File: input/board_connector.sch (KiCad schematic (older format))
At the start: 1 part

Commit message: Still beating into overall shape.  This is a checkpoint before modifying the analog signal chain to fold the diff amp and antialias into the driver, going to a full differential path.
Overall: Changes to component attributes to reduce duplicates in BOM, and added links to Digikey and datasheets.

board_connector.sch: Added reference input pins, decimation SEL lines.

in_filter.sch:
Fixed BIST feedback to be taken at the top of each injection resistor (4 lines, not 2)

input_board.sch:
Added some missing connections and no-connects.

power_budget.xlsx:
Much more elaborate now, models effect of input levels on load currents, computes currents and total power, for several variants.

reference_buffer.sch:
Updated with booster sink transistor to handle sourcing into reference by ADC clamp diodes.

simetrix/:
Added supply_negative.wxsch and supply_positive.wxsch, which are concepts for low noise lowish dropout regulators for the analog rails.  Other simetrix modifications are cosmetic.
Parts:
- J2: renamed from J?; footprint Connector_PinHeader_2.54mm:PinHeader_2x32_P2.54mm_Vertical -> Connector_DIN:DIN41612_B_2x32_Horizontal; Description (none) -> 64 Position Din Connector Header, Male Pins Gold Through Ho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; Digikey (none) -> 609-5856-ND; MPN (none) -> 86092645113755ELF; Notes (none) -> Eurocard type B
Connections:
- net labels added: +reference, -reference, SEL0, SEL1, SYNC_IN
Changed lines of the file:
@@
 Comment4 ""
 $EndDescr
-$Sheet
-S 7850 1800 1100 450
-U 5E1DA2AA
-F0 "sheet5E1DA2A6" 50
-F1 "reference_buffer.sch" 50
-F2 "-reference" I L 7850 2100 50
-F3 "+reference" I L 7850 1950 50
-$EndSheet
 Text Notes 7250 6800 0    50   ~ 0
 The connector to the main board, and other support circuitry that\nconnects by global labels
@@
 P 1150 4200
 AR Path="/5E1D6B84" Ref="J?"  Part="1"
-AR Path="/5E1D6729/5E1D6B84" Ref="J?"  Part="1"
-F 0 "J?" H 1150 7550 50  0000 C CNN
+AR Path="/5E1D6729/5E1D6B84" Ref="J2"  Part="1"
+F 0 "J2" H 1150 7550 50  0000 C CNN
 F 1 "C64AB" V 1400 4250 50  0000 C CNN
-F 2 "Connector_PinHeader_2.54mm:PinHeader_2x32_P2.54mm_Vertical" H 1150 4250 50  0001 C CNN
+F 2 "Connector_DIN:DIN41612_B_2x32_Horizontal" H 1150 4250 50  0001 C CNN
 F 3 " ~" H 1150 4250 50  0001 C CNN
+F 4 "64 Position Din Connector Header, Male Pins Gold Through Hole, Right Angle" H 1150 4200 50  0001 C CNN "Description"
+F 5 "609-5856-ND" H 1150 4200 50  0001 C CNN "Digikey"
+F 6 "86092645113755ELF" H 1150 4200 50  0001 C CNN "MPN"
+F 7 "Eurocard type B" H 1150 4200 50  0001 C CNN "Notes"
 	1    1150 4200
 	-1   0    0    -1
 $EndComp
 $Comp
-L power:GNDD #PWR?
+L power:GNDD #PWR011
 U 1 1 5E271928
 P 1900 4000
-F 0 "#PWR?" H 1900 3750 50  0001 C CNN
+F 0 "#PWR011" H 1900 3750 50  0001 C CNN
 F 1 "GNDD" H 1900 3875 50  0000 C CNN
 F 2 "" H 1900 4000 50  0001 C CNN
@@
 	1600 4100 1600 4000
 $Comp
-L power:+5VD #PWR?
+L power:+5VD #PWR012
 U 1 1 5E27F010
 P 2200 4300
-F 0 "#PWR?" H 2200 4150 50  0001 C CNN
+F 0 "#PWR012" H 2200 4150 50  0001 C CNN
 F 1 "+5VD" H 2200 4440 50  0000 C CNN
 F 2 "" H 2200 4300 50  0001 C CNN
@@
 	2200 4300 1700 4300
 Connection ~ 1700 4300
+Text GLabel 3000 6650 2    50   Output ~ 0
++reference
+Text GLabel 3000 6800 2    50   Output ~ 0
+-reference
+Text GLabel 2450 4650 2    50   Output ~ 0
+SYNC_IN
+Text GLabel 3300 5600 0    50   Input ~ 0
+SEL0
+Text GLabel 3300 5700 0    50   Input ~ 0
+SEL1
 $EndSCHEMATC

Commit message: Mostly work on power, regulators and distribution.  Also more BOM cleanup.
All of the bypass capacitors are now spec'd and in the DigiKey BOM. TVS zeners are now
spec'd.  Folded together some resistor values and got rid of some 1206 parts that no longer
need that much power rating at the lower supplies.

A affecting all of the input channel sheets is that we now distribute filtered V+, V- and VREF
via sheet ports.  The V+, V- filter is on input_channel.sch and the VREF filter is still in
adc.sch, but is distributed out to the other sheets that need it.

bist_buffer.sch: added buffer for built-in self-test

board_connector.sch: put the input filter for the analog supplies here.

power.sch: added regulators for the supplies.

reference_buffer.sch:
changed components to match those chosen for the V+, V- regulators and added
current steering diodes to bootstrap the reference buffer supply.  This is
necessary because the analog supplies are now derived from VREF.

*.wxsch:
Updates to spice models related to work on supplies.
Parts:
- added C16, C17, C18, C19: 1uF, Capacitor_SMD:C_0805_2012Metric, symbol Device:C_Small
- added C20, C21: 330uF, Capacitor_SMD:CP_Elec_8x6.7, symbol Device:CP1_Small
- added D8, D9: 10V (standoff), Diode_SMD:D_SMA, symbol Device:D_Zener
- added FB1, FB2: 21 Ohm, digikey-footprints:0805, symbol dk_Ferrite-Beads-and-Chips:MPZ2012S601AT000
- added FL1: 100uH, symbol ilemt_input:EMI_Filter_CommonMode_3Line
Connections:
- net labels added: BIST++_IN, BIST+-_IN, BIST-+_IN, BIST--_IN, GNDA, RAW_+5VANA, RAW_+5VDIG, RAW_V+, RAW_V-
- net labels removed: +5VD
- wire segments 54 -> 95

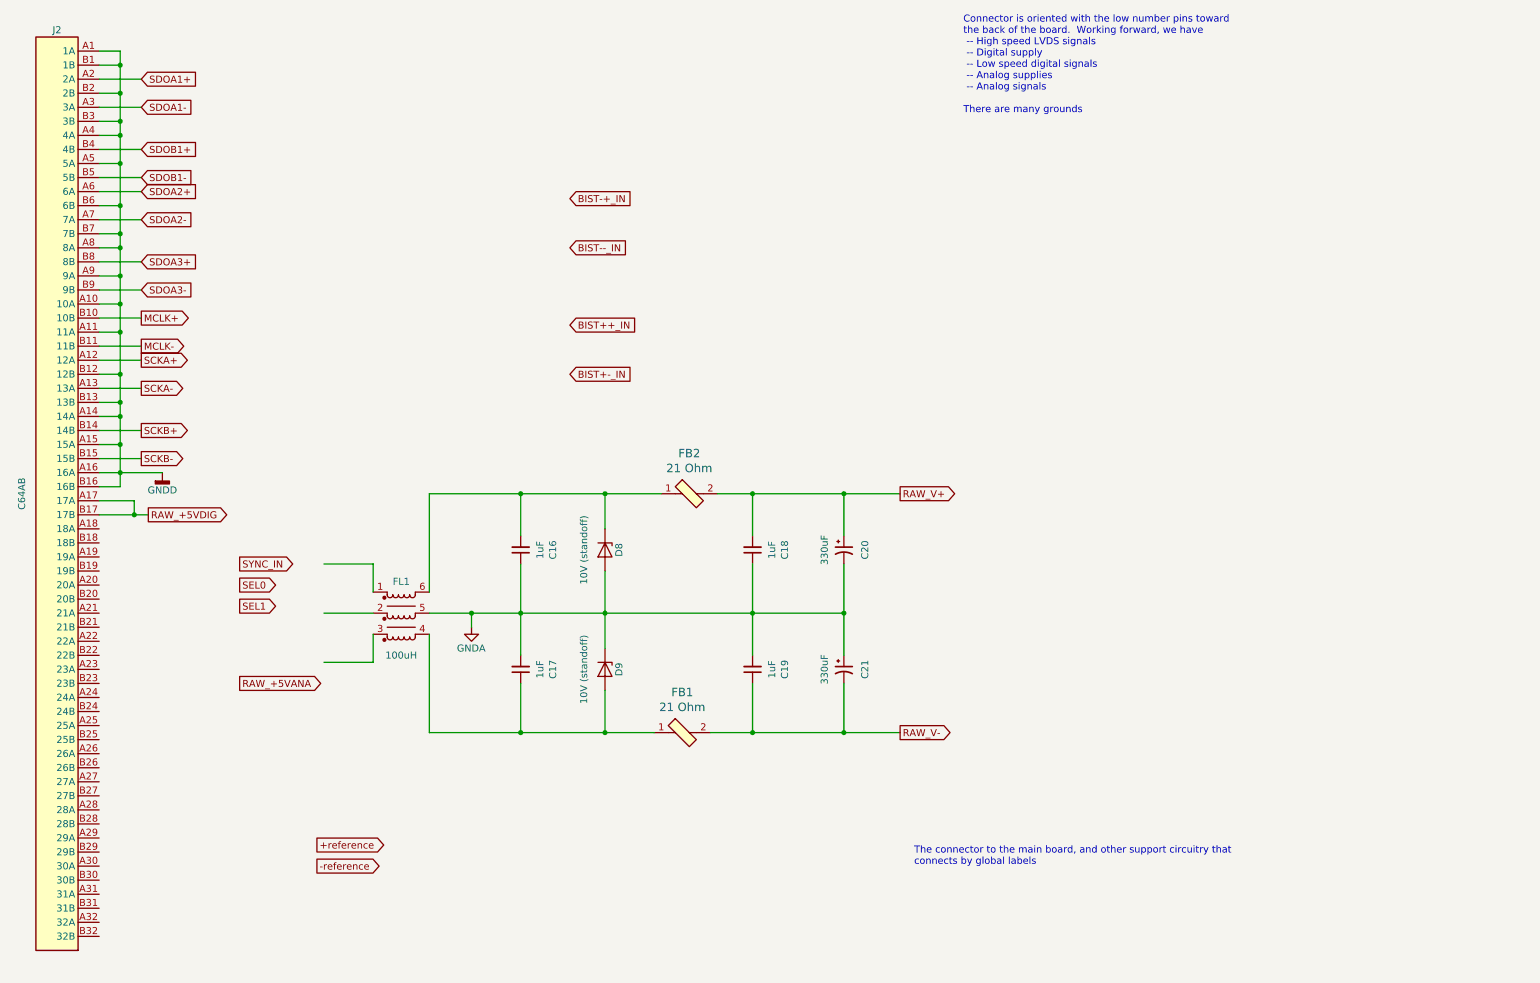
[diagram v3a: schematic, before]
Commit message: Mostly finished wiring.
Finished mapping pins in board_connector.sch.  Renamed some nets and moved the analog
supply filter to power.sch.  Added probe_connector.sch which now includes input protected
on the probe calibration one-wire line.  The configuration digital interface stuff is still
sketchy, this is basically a placeholder.  Eventually we will have an I2C I/O extender for
configuration and calibration memory, but for now I added a jumper header for setting the
SEL0/SEL1 lines to control the ADC decimation.
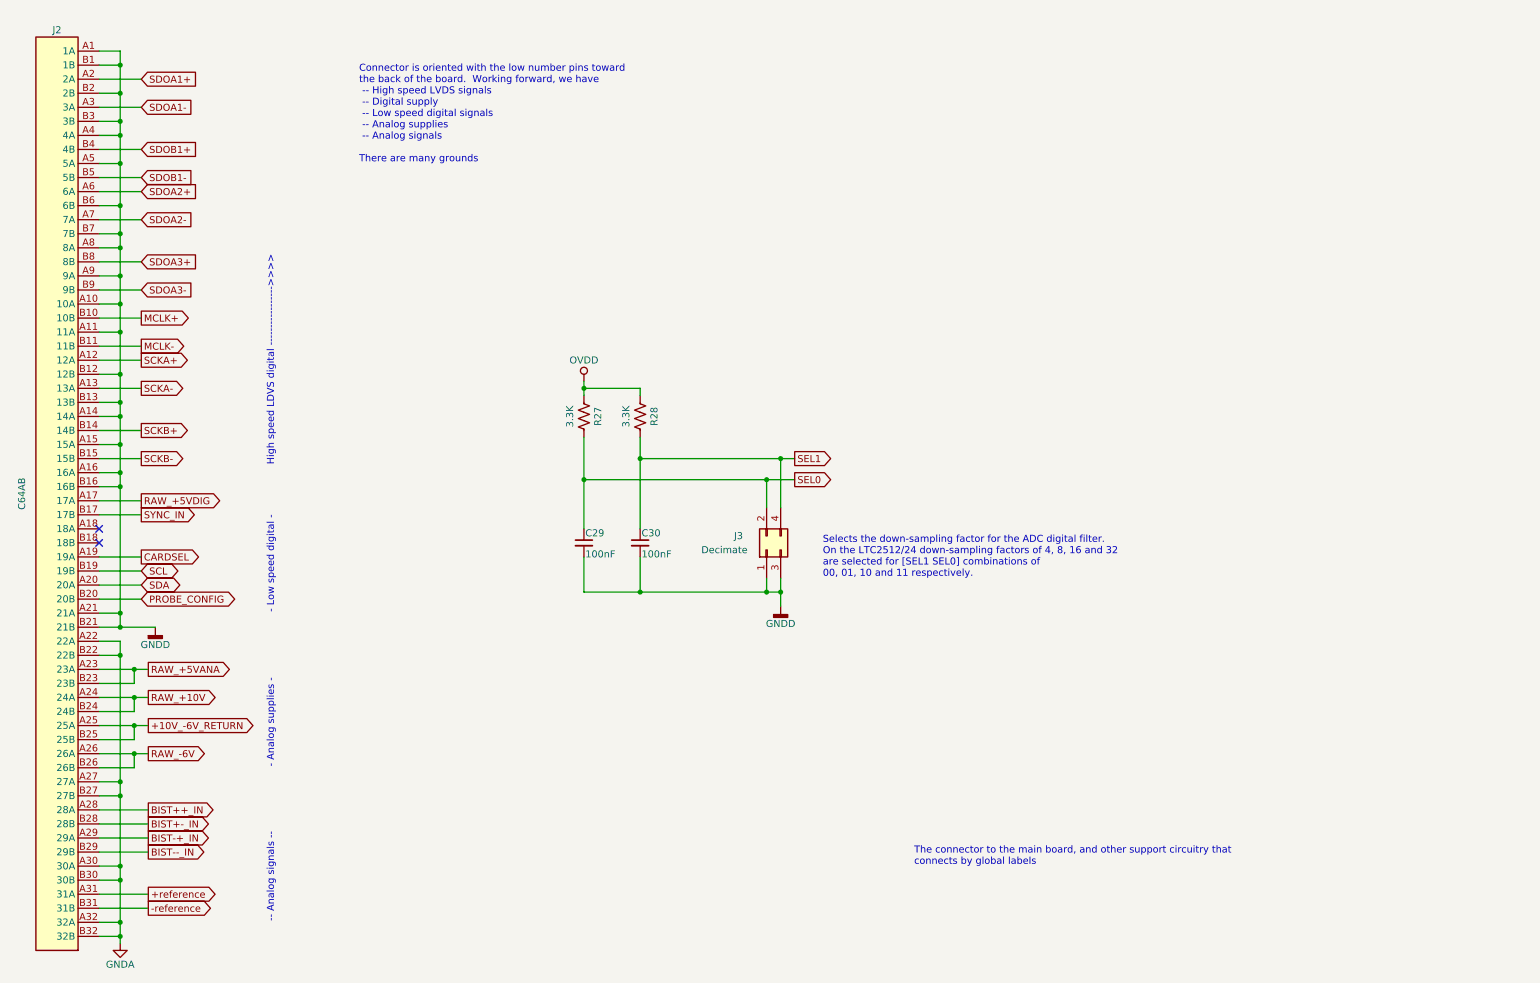
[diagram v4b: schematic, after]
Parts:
- removed C16, C17, C18, C19: 1uF, Capacitor_SMD:C_0805_2012Metric, symbol Device:C_Small
- removed C20, C21: 330uF, Capacitor_SMD:CP_Elec_8x6.7, symbol Device:CP1_Small
- removed D8, D9: 10V (standoff), Diode_SMD:D_SMA, symbol Device:D_Zener
- removed FB1, FB2: 21 Ohm, digikey-footprints:0805, symbol dk_Ferrite-Beads-and-Chips:MPZ2012S601AT000
- removed FL1: 100uH, symbol ilemt_input:EMI_Filter_CommonMode_3Line
- added C29, C30: 100nF, Capacitor_SMD:C_0603_1608Metric, symbol Device:C_Small
- added J3: Decimate, symbol Connector_Generic:Conn_02x02_Odd_Even
- added R27, R28: 3.3K, Resistor_SMD:R_0603_1608Metric, symbol Device:R_US
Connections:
- net labels added: +10V_-6V_RETURN, CARDSEL, OVDD, PROBE_CONFIG, RAW_+10V, RAW_-6V, SCL, SDA
- net labels removed: RAW_V+, RAW_V-
- wire segments 95 -> 120
- no-connect marks 0 -> 2
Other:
- note added: "- Analog supplies -"
- note added: "- Low speed digital -"
- note added: "-- Analog signals --"
- note added: "High speed LDVS digital ----------------->>>>"
- note added: "Selects the down-sampling factor for the ADC digital filter. \nOn the LTC2512/24 down-sampling factors of 4, 8, 16 and 32 \nare selected for [SEL1 SEL0] combinations of \n00, 01, 10 and 11 respectively."

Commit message: Cleanup to get ready to start board layout. I had to get rid off all the bus signals, since in Kicad busses don't work that way.  Added a couple testpoints; many more needed.
Work on component placement in PCB.  I changed DGND to plain GND and "protective earth" to
"earth" (for chassis ground).  Chassis ground is now connected on the board only via a capacitor.
I had to fix the connector footprint to match the pin numbers on the symbol (there was a case
difference).
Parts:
- J2: symbol Connector:C64AB -> ilemt_input:my_C64AB
- J3: footprint (none) -> Connector_PinHeader_2.00mm:PinHeader_2x02_P2.00mm_Vertical_SMD; Description (none) -> CONN HEADER SMD 4POS 2MM; Digikey (none) -> S6009-02-ND
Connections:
- net +10V_-6V_RETURN: now also J2.a25 (25A), J2.b25 (25B); no longer J2.A25 (25A), J2.B25 (25B)
- net +reference: now also J2.a31 (31A); no longer J2.A31 (31A)
- net -reference: now also J2.b31 (31B); no longer J2.B31 (31B)
- net BIST++_IN: now also J2.a28 (28A); no longer J2.A28 (28A)
- net BIST+-_IN: now also J2.b28 (28B); no longer J2.B28 (28B)
- net BIST-+_IN: now also J2.a29 (29A); no longer J2.A29 (29A)
- net BIST--_IN: now also J2.b29 (29B); no longer J2.B29 (29B)
- net CARDSEL: now also J2.a19 (19A); no longer J2.A19 (19A)
- net GNDA: now also J2.a22 (22A), J2.a27 (27A), J2.a30 (30A), J2.a32 (32A), J2.b22 (22B), J2.b27 (27B), J2.b30 (30B), J2.b32 (32B); no longer J2.A22 (22A), J2.A27 (27A), J2.A30 (30A), J2.A32 (32A), J2.B22 (22B), J2.B27 (27B), J2.B30 (30B), J2.B32 (32B)
- net MCLK+: now also J2.b10 (10B); no longer J2.B10 (10B)
- net MCLK-: now also J2.b11 (11B); no longer J2.B11 (11B)
- net PROBE_CONFIG: now also J2.b20 (20B); no longer J2.B20 (20B)
- net RAW_+10V: now also J2.a24 (24A), J2.b24 (24B); no longer J2.A24 (24A), J2.B24 (24B)
- net RAW_+5VANA: now also J2.a23 (23A), J2.b23 (23B); no longer J2.A23 (23A), J2.B23 (23B)
- net RAW_+5VDIG: now also J2.a17 (17A); no longer J2.A17 (17A)
- net RAW_-6V: now also J2.a26 (26A), J2.b26 (26B); no longer J2.A26 (26A), J2.B26 (26B)
- net SCKA+: now also J2.a12 (12A); no longer J2.A12 (12A)
- net SCKA-: now also J2.a13 (13A); no longer J2.A13 (13A)
- net SCKB+: now also J2.b14 (14B); no longer J2.B14 (14B)
- net SCKB-: now also J2.b15 (15B); no longer J2.B15 (15B)
- net SCL: now also J2.b19 (19B); no longer J2.B19 (19B)
- net SDA: now also J2.a20 (20A); no longer J2.A20 (20A)
- net SDOA1+: now also J2.a2 (2A); no longer J2.A2 (2A)
- net SDOA1-: now also J2.a3 (3A); no longer J2.A3 (3A)
- net SDOA2+: now also J2.a6 (6A); no longer J2.A6 (6A)
- net SDOA2-: now also J2.a7 (7A); no longer J2.A7 (7A)
- net SDOA3+: now also J2.b8 (8B); no longer J2.B8 (8B)
- net SDOA3-: now also J2.b9 (9B); no longer J2.B9 (9B)
- net SDOB1+: now also J2.b4 (4B); no longer J2.B4 (4B)
- net SDOB1-: now also J2.b5 (5B); no longer J2.B5 (5B)
- net SYNC_IN: now also J2.b17 (17B); no longer J2.B17 (17B)
- removed net GNDD: C29.2, C30.2, J2.A1 (1A), J2.A10 (10A), J2.A11 (11A), J2.A14 (14A), J2.A15 (15A), J2.A16 (16A), J2.A21 (21A), J2.A4 (4A), J2.A5 (5A), J2.A8 (8A), J2.A9 (9A), J2.B1 (1B), J2.B12 (12B), J2.B13 (13B), J2.B16 (16B), J2.B2 (2B), J2.B21 (21B), J2.B3 (3B), J2.B6 (6B), J2.B7 (7B), J3.1 (Pin_1), J3.3 (Pin_3)
- new net GND: C29.2, C30.2, J2.a1 (1A), J2.a10 (10A), J2.a11 (11A), J2.a14 (14A), J2.a15 (15A), J2.a16 (16A), J2.a21 (21A), J2.a4 (4A), J2.a5 (5A), J2.a8 (8A), J2.a9 (9A), J2.b1 (1B), J2.b12 (12B), J2.b13 (13B), J2.b16 (16B), J2.b2 (2B), J2.b21 (21B), J2.b3 (3B), J2.b6 (6B), J2.b7 (7B), J3.1 (Pin_1), J3.3 (Pin_3)
- no-connect marks 2 -> 5
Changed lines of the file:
@@
 SDOA1+
 $Comp
-L Connector:C64AB J?
+L ilemt_input:my_C64AB J?
 U 1 1 5E1D6B84
 P 1150 4200
@@
 	1    1150 4200
 	-1   0    0    -1
-$EndComp
-$Comp
-L power:GNDD #PWR011
-U 1 1 5E271928
-P 1850 5100
-F 0 "#PWR011" H 1850 4850 50  0001 C CNN
-F 1 "GNDD" H 1850 4975 50  0000 C CNN
-F 2 "" H 1850 5100 50  0001 C CNN
-F 3 "" H 1850 5100 50  0001 C CNN
-	1    1850 5100
-	1    0    0    -1
 $EndComp
 Wire Wire Line
@@
 F 0 "J3" V 6300 4750 50  0000 C CNN
 F 1 "Decimate" V 6200 4850 50  0000 C CNN
-F 2 "" H 6200 4550 50  0001 C CNN
+F 2 "Connector_PinHeader_2.00mm:PinHeader_2x02_P2.00mm_Vertical_SMD" H 6200 4550 50  0001 C CNN
 F 3 "~" H 6200 4550 50  0001 C CNN
+F 4 "CONN HEADER SMD 4POS 2MM" H 6200 4550 50  0001 C CNN "Description"
+F 5 "S6009-02-ND" H 6200 4550 50  0001 C CNN "Digikey"
 	1    6200 4550
 	0    -1   -1   0
@@
 Wire Wire Line
 	6200 4250 6200 4050
-$Comp
-L power:GNDD #PWR046
-U 1 1 5E72EE51
-P 6300 4950
-F 0 "#PWR046" H 6300 4700 50  0001 C CNN
-F 1 "GNDD" H 6300 4825 50  0000 C CNN
-F 2 "" H 6300 4950 50  0001 C CNN
-F 3 "" H 6300 4950 50  0001 C CNN
-	1    6300 4950
-	1    0    0    -1
-$EndComp
 Wire Wire Line
 	6200 4750 6200 4850
@@
 Wire Wire Line
 	5300 4850 6200 4850
+NoConn ~ 1450 4600
+NoConn ~ 1450 4700
+NoConn ~ 1450 4800
+$Comp
+L power:GND #PWR0148
+U 1 1 5E303199
+P 1850 5100
+F 0 "#PWR0148" H 1850 4850 50  0001 C CNN
+F 1 "GND" H 1850 4950 50  0000 C CNN
+F 2 "" H 1850 5100 50  0001 C CNN
+F 3 "" H 1850 5100 50  0001 C CNN
+	1    1850 5100
+	1    0    0    -1
+$EndComp
+$Comp
+L power:GND #PWR0149
+U 1 1 5E3037B0
+P 6300 4950
+F 0 "#PWR0149" H 6300 4700 50  0001 C CNN
+F 1 "GND" H 6300 4800 50  0000 C CNN
+F 2 "" H 6300 4950 50  0001 C CNN
+F 3 "" H 6300 4950 50  0001 C CNN
+	1    6300 4950
+	1    0    0    -1
+$EndComp
 $EndSCHEMATC
